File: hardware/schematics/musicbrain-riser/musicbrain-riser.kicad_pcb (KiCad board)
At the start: 2 copper layers, 31 x 80 mm, 2 parts, among them J1 BUS, J2 NAAR FRONT

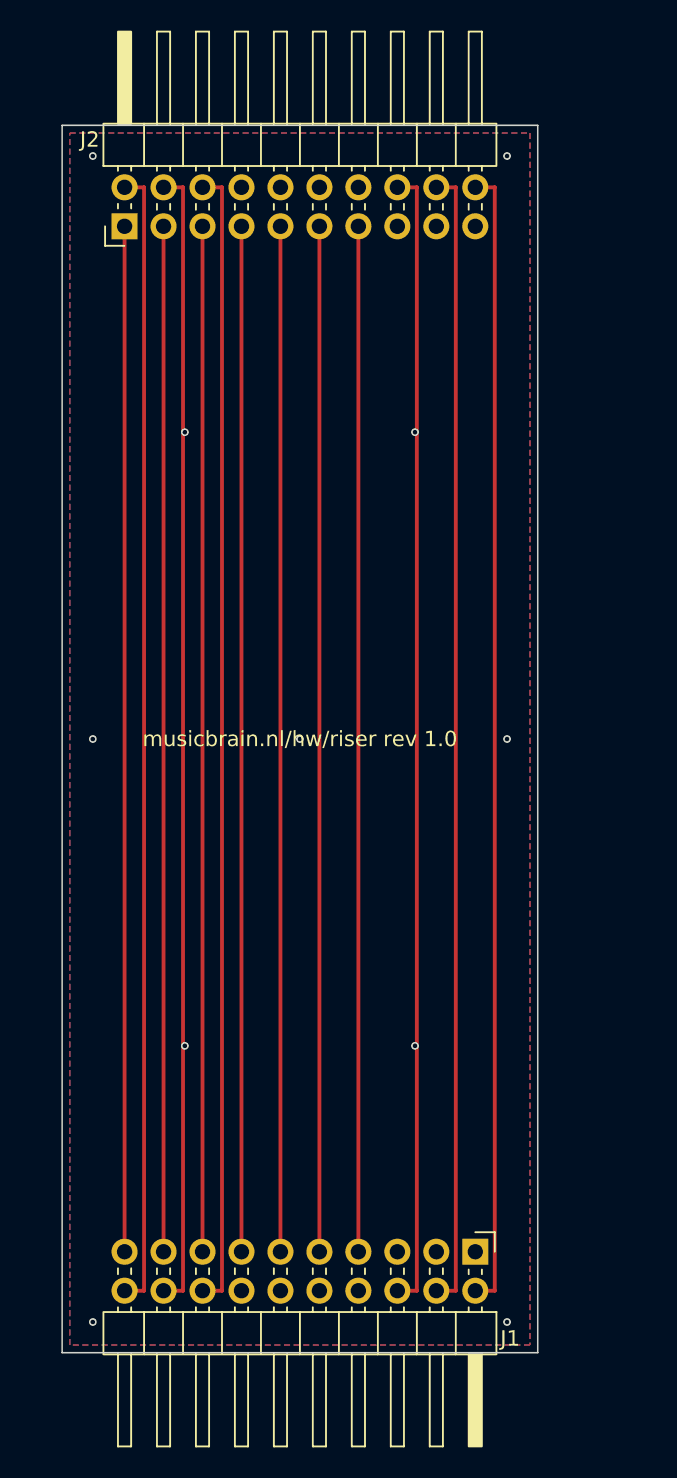
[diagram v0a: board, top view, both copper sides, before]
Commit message: Gen 2 stap 3b/3c: riser + potriser rev 2.0 (2x12, H=50) DRC 0/0
riser: 40x50, hele 2x12-bus 1-op-1 omhoog incl. de audio-lijnen ->
ontwikkelbord voor een gedelegeerde Teensy/FPGA. x-matching schaalt mee:
J2-pin q draagt slotfunctie (24-q) oneven / (26-q) even.

potriser: 28x80 -> 80x50, J1 2x12; koper via freerouting i.p.v. handlanen
(1 unrouted -> snap_stubs dichtte 'm). Front-contract 1x10 ongewijzigd.

Meetvondst: de connector-bodies hangen bewust OVER de bordrand (zo mateert
de kaart met de socket eronder) -- dus de vrije kernband bij H=50 is 33,3 mm,
niet 18,8 zoals ik eerst schatte. Daarmee komt elke kaart op 80x50 uit op
5-16% dichtheid (adc8, de drukste: 15,6%) -- lager dan de huidige ~17% op
80 mm hoog. H=50 is dus ruim haalbaar voor alle kaarten.

Alle drie de risers: ERC 0 / netcheck OK / DRC 0/0.

Co-Authored-By: Claude Fable 5 <noreply@anthropic.com>
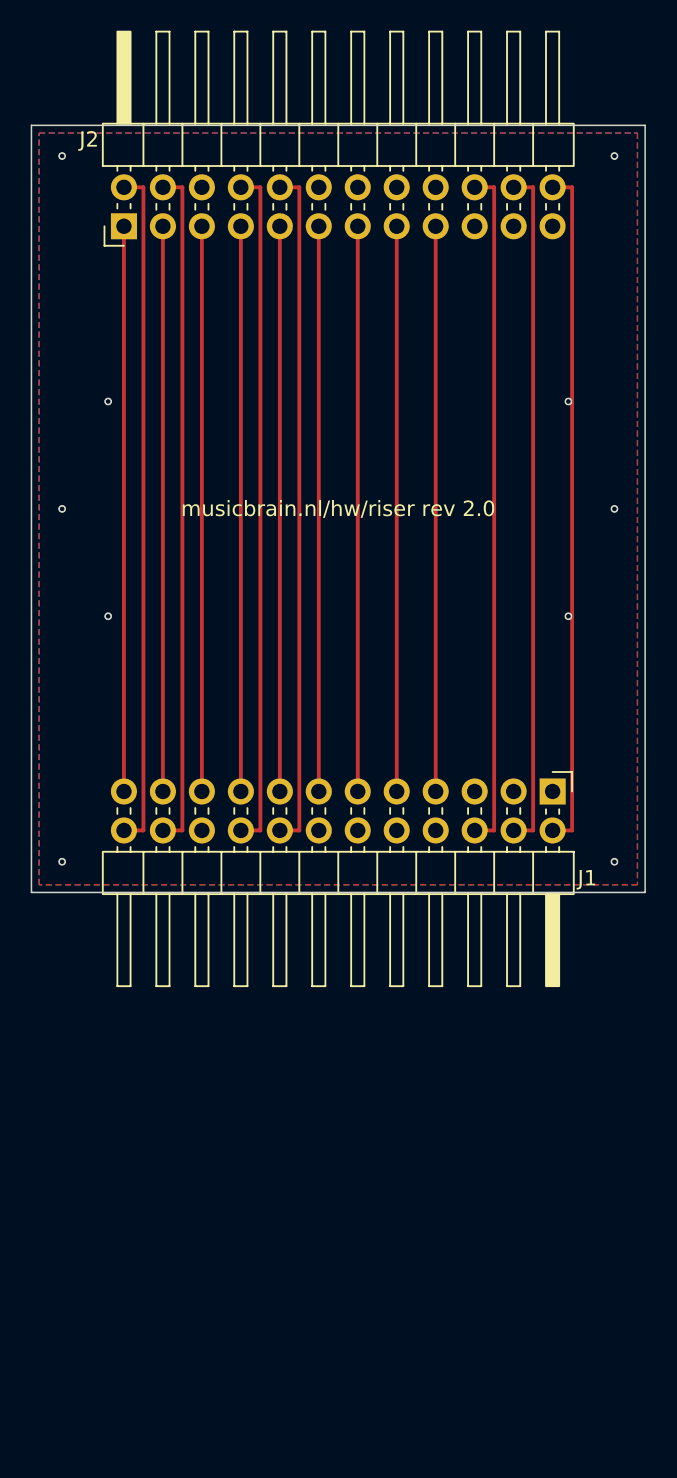
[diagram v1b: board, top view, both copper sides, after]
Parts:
- J1, J2: footprint Connector_PinHeader_2.54mm:PinHeader_2x10_P2.54mm_Horizontal -> Connector_PinHeader_2.54mm:PinHeader_2x12_P2.54mm_Horizontal
- moved J1 30.4 mm to (134.0, 143.4)
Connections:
- J1 pad 20: /SPARE2 -> GND
- J2 pad 1: /SPARE1 -> /LRCLK
- J2 pad 10: GND -> /IRQ
- J2 pad 11: /MOSI -> /CS
- J2 pad 13: /SCLK -> /MISO
- J2 pad 15: GND -> /MOSI
- J2 pad 16: +3V3 -> GND
- J2 pad 17: GND -> /SCLK
- J2 pad 18: -12V -> GND
- J2 pad 2: /SPARE2 -> /I2S_DATA
- J2 pad 20: +12V -> +3V3
- J2 pad 3: /SDA -> /MCLK
- J2 pad 4: /SCL -> /BCLK
- J2 pad 5: /LDAC -> /SPARE1
- J2 pad 6: /IRQ -> GND
- J2 pad 7: /CS -> /SDA
- J2 pad 8: GND -> /SCL
- J2 pad 9: /MISO -> /LDAC
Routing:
- net /SPARE2: track 74.5 -> 0.00 mm
- net /BCLK: track 0.00 -> 44.5 mm
- net /I2S_DATA: track 0.00 -> 44.5 mm
- net /MCLK: track 0.00 -> 36.8 mm
- net /LRCLK: track 0.00 -> 36.8 mm
- net -12V: track 74.5 -> 44.5 mm
- net /SPARE1: track 66.8 -> 36.8 mm
- net /SDA: track 66.8 -> 36.8 mm
- net /SCLK: track 66.8 -> 36.8 mm
- net /SCL: track 74.5 -> 44.5 mm
- net /MOSI: track 66.8 -> 36.8 mm
- net /MISO: track 66.8 -> 36.8 mm
- net /LDAC: track 66.8 -> 36.8 mm
- net /IRQ: track 74.5 -> 44.5 mm
- net /CS: track 66.8 -> 36.8 mm
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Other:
- board size 31 x 80 mm -> 40 x 50 mm
- board text added: "musicbrain.nl/hw/riser rev 2.0"
- board text removed: "musicbrain.nl/hw/riser rev 1.0"

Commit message: gen 2: kaarthoogte 50 -> 45 mm; potriser-herroute (U1 rot 270)
- bus.py: H=45 (band 30,84 mm = bewezen gen-1-dichtheid)
- gen_riser/gen_i2criser/gen_potriser: y-literals geparametriseerd op
  bus.BY0/BY1; potriser leest nu ook gnd_stitch.json in
- potriser: U1 rot 90 -> 270 (kanalen noord, SPI+GND zuid) - bij rot 90
  wikkelden de wiper-banen zich om pad 14 (AGND) en raakte die los van
  het vlak; nieuwe freerouting (0 unrouted) + 1 hechtvia
- alle drie risers: ERC 0, netcheck OK, DRC 0/0 op 40x45 (potriser 80x45)
- docs: spi-bus-spec + systeem-v3-plan H=50 -> H=45, jack4-kabelnotitie

Co-Authored-By: Claude Fable 5 <noreply@anthropic.com>
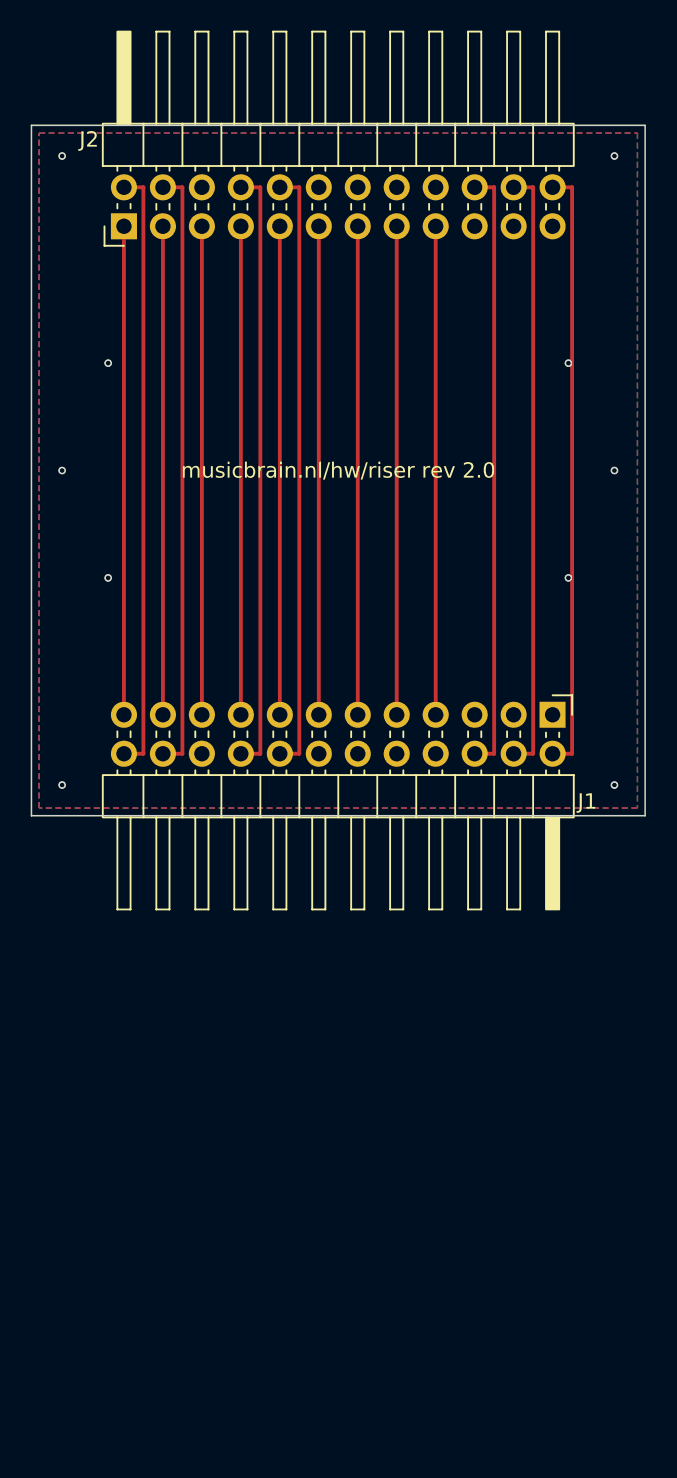
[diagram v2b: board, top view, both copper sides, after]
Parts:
- moved J1 5.00 mm to (134.0, 138.4)
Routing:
- net /SPARE1: track 36.8 -> 31.8 mm
- net /SDA: track 36.8 -> 31.8 mm
- net /SCLK: track 36.8 -> 31.8 mm
- net /SCL: track 44.5 -> 39.5 mm
- net /MOSI: track 36.8 -> 31.8 mm
- net /MISO: track 36.8 -> 31.8 mm
- net /MCLK: track 36.8 -> 31.8 mm
- net /LRCLK: track 36.8 -> 31.8 mm
- net /LDAC: track 36.8 -> 31.8 mm
- net /IRQ: track 44.5 -> 39.5 mm
- net /I2S_DATA: track 44.5 -> 39.5 mm
- net /CS: track 36.8 -> 31.8 mm
- net /BCLK: track 44.5 -> 39.5 mm
- net -12V: track 44.5 -> 39.5 mm
- net +3V3: track 44.5 -> 39.5 mm
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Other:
- board size 40 x 50 mm -> 40 x 45 mm
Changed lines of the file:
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@@
   (net 17 "GND")
   (footprint "Connector_PinHeader_2.54mm:PinHeader_2x12_P2.54mm_Horizontal"
-    (at 133.97 143.42 270)
+    (at 133.97 138.42 270)
     (layer "F.Cu")
     (descr "Through hole angled pin header, 2x12, 2.54mm pitch, 6mm pin length, double rows")
@@
     )
   )
-  (segment (start 133.97 145.96) (end 135.24 145.96) (width 0.25) (layer "F.Cu") (net 1))
-  (segment (start 135.24 145.96) (end 135.24 104.04) (width 0.25) (layer "F.Cu") (net 1))
+  (segment (start 133.97 140.96) (end 135.24 140.96) (width 0.25) (layer "F.Cu") (net 1))
+  (segment (start 135.24 140.96) (end 135.24 104.04) (width 0.25) (layer "F.Cu") (net 1))
   (segment (start 135.24 104.04) (end 133.97 104.04) (width 0.25) (layer "F.Cu") (net 1))
-  (segment (start 131.43 145.96) (end 132.7 145.96) (width 0.25) (layer "F.Cu") (net 3))
-  (segment (start 132.7 145.96) (end 132.7 104.04) (width 0.25) (layer "F.Cu") (net 3))
+  (segment (start 131.43 140.96) (end 132.7 140.96) (width 0.25) (layer "F.Cu") (net 3))
+  (segment (start 132.7 140.96) (end 132.7 104.04) (width 0.25) (layer "F.Cu") (net 3))
   (segment (start 132.7 104.04) (end 131.43 104.04) (width 0.25) (layer "F.Cu") (net 3))
-  (segment (start 128.89 145.96) (end 130.16 145.96) (width 0.25) (layer "F.Cu") (net 2))
-  (segment (start 130.16 145.96) (end 130.16 104.04) (width 0.25) (layer "F.Cu") (net 2))
+  (segment (start 128.89 140.96) (end 130.16 140.96) (width 0.25) (layer "F.Cu") (net 2))
+  (segment (start 130.16 140.96) (end 130.16 104.04) (width 0.25) (layer "F.Cu") (net 2))
   (segment (start 130.16 104.04) (end 128.89 104.04) (width 0.25) (layer "F.Cu") (net 2))
-  (segment (start 126.35 143.42) (end 126.35 106.58) (width 0.25) (layer "F.Cu") (net 14))
-  (segment (start 123.81 143.42) (end 123.81 106.58) (width 0.25) (layer "F.Cu") (net 12))
-  (segment (start 121.27 143.42) (end 121.27 106.58) (width 0.25) (layer "F.Cu") (net 11))
-  (segment (start 118.73 143.42) (end 118.73 106.58) (width 0.25) (layer "F.Cu") (net 5))
-  (segment (start 116.19 143.42) (end 116.19 106.58) (width 0.25) (layer "F.Cu") (net 8))
-  (segment (start 116.19 145.96) (end 117.46 145.96) (width 0.25) (layer "F.Cu") (net 7))
-  (segment (start 117.46 145.96) (end 117.46 104.04) (width 0.25) (layer "F.Cu") (net 7))
+  (segment (start 126.35 138.42) (end 126.35 106.58) (width 0.25) (layer "F.Cu") (net 14))
+  (segment (start 123.81 138.42) (end 123.81 106.58) (width 0.25) (layer "F.Cu") (net 12))
+  (segment (start 121.27 138.42) (end 121.27 106.58) (width 0.25) (layer "F.Cu") (net 11))
+  (segment (start 118.73 138.42) (end 118.73 106.58) (width 0.25) (layer "F.Cu") (net 5))
+  (segment (start 116.19 138.42) (end 116.19 106.58) (width 0.25) (layer "F.Cu") (net 8))
+  (segment (start 116.19 140.96) (end 117.46 140.96) (width 0.25) (layer "F.Cu") (net 7))
+  (segment (start 117.46 140.96) (end 117.46 104.04) (width 0.25) (layer "F.Cu") (net 7))
   (segment (start 117.46 104.04) (end 116.19 104.04) (width 0.25) (layer "F.Cu") (net 7))
-  (segment (start 113.65 143.42) (end 113.65 106.58) (width 0.25) (layer "F.Cu") (net 15))
-  (segment (start 113.65 145.96) (end 114.92 145.96) (width 0.25) (layer "F.Cu") (net 13))
-  (segment (start 114.92 145.96) (end 114.92 104.04) (width 0.25) (layer "F.Cu") (net 13))
+  (segment (start 113.65 138.42) (end 113.65 106.58) (width 0.25) (layer "F.Cu") (net 15))
+  (segment (start 113.65 140.96) (end 114.92 140.96) (width 0.25) (layer "F.Cu") (net 13))
+  (segment (start 114.92 140.96) (end 114.92 104.04) (width 0.25) (layer "F.Cu") (net 13))
   (segment (start 114.92 104.04) (end 113.65 104.04) (width 0.25) (layer "F.Cu") (net 13))
-  (segment (start 111.11 143.42) (end 111.11 106.58) (width 0.25) (layer "F.Cu") (net 16))
-  (segment (start 108.57 143.42) (end 108.57 106.58) (width 0.25) (layer "F.Cu") (net 10))
-  (segment (start 108.57 145.96) (end 109.84 145.96) (width 0.25) (layer "F.Cu") (net 4))
-  (segment (start 109.84 145.96) (end 109.84 104.04) (width 0.25) (layer "F.Cu") (net 4))
+  (segment (start 111.11 138.42) (end 111.11 106.58) (width 0.25) (layer "F.Cu") (net 16))
+  (segment (start 108.57 138.42) (end 108.57 106.58) (width 0.25) (layer "F.Cu") (net 10))
+  (segment (start 108.57 140.96) (end 109.84 140.96) (width 0.25) (layer "F.Cu") (net 4))
+  (segment (start 109.84 140.96) (end 109.84 104.04) (width 0.25) (layer "F.Cu") (net 4))
   (segment (start 109.84 104.04) (end 108.57 104.04) (width 0.25) (layer "F.Cu") (net 4))
-  (segment (start 106.03 143.42) (end 106.03 106.58) (width 0.25) (layer "F.Cu") (net 9))
-  (segment (start 106.03 145.96) (end 107.3 145.96) (width 0.25) (layer "F.Cu") (net 6))
-  (segment (start 107.3 145.96) (end 107.3 104.04) (width 0.25) (layer "F.Cu") (net 6))
+  (segment (start 106.03 138.42) (end 106.03 106.58) (width 0.25) (layer "F.Cu") (net 9))
+  (segment (start 106.03 140.96) (end 107.3 140.96) (width 0.25) (layer "F.Cu") (net 6))
+  (segment (start 107.3 140.96) (end 107.3 104.04) (width 0.25) (layer "F.Cu") (net 6))
   (segment (start 107.3 104.04) (end 106.03 104.04) (width 0.25) (layer "F.Cu") (net 6))
   (via (at 102 102) (size 0.5) (drill 0.3) (layers "F.Cu" "B.Cu") (net 17))
   (via (at 138 102) (size 0.5) (drill 0.3) (layers "F.Cu" "B.Cu") (net 17))
-  (via (at 102 148) (size 0.5) (drill 0.3) (layers "F.Cu" "B.Cu") (net 17))
-  (via (at 138 148) (size 0.5) (drill 0.3) (layers "F.Cu" "B.Cu") (net 17))
-  (via (at 102 125) (size 0.5) (drill 0.3) (layers "F.Cu" "B.Cu") (net 17))
-  (via (at 138 125) (size 0.5) (drill 0.3) (layers "F.Cu" "B.Cu") (net 17))
-  (via (at 105 118) (size 0.5) (drill 0.3) (layers "F.Cu" "B.Cu") (net 17))
-  (via (at 135 118) (size 0.5) (drill 0.3) (layers "F.Cu" "B.Cu") (net 17))
-  (via (at 105 132) (size 0.5) (drill 0.3) (layers "F.Cu" "B.Cu") (net 17))
-  (via (at 135 132) (size 0.5) (drill 0.3) (layers "F.Cu" "B.Cu") (net 17))
-  (gr_rect (start 100.0 100.0) (end 140.0 150.0)
+  (via (at 102 143) (size 0.5) (drill 0.3) (layers "F.Cu" "B.Cu") (net 17))
+  (via (at 138 143) (size 0.5) (drill 0.3) (layers "F.Cu" "B.Cu") (net 17))
+  (via (at 102 122.5) (size 0.5) (drill 0.3) (layers "F.Cu" "B.Cu") (net 17))
+  (via (at 138 122.5) (size 0.5) (drill 0.3) (layers "F.Cu" "B.Cu") (net 17))
+  (via (at 105 115.5) (size 0.5) (drill 0.3) (layers "F.Cu" "B.Cu") (net 17))
+  (via (at 135 115.5) (size 0.5) (drill 0.3) (layers "F.Cu" "B.Cu") (net 17))
+  (via (at 105 129.5) (size 0.5) (drill 0.3) (layers "F.Cu" "B.Cu") (net 17))
+  (via (at 135 129.5) (size 0.5) (drill 0.3) (layers "F.Cu" "B.Cu") (net 17))
+  (gr_rect (start 100.0 100.0) (end 140.0 145.0)
     (stroke (width 0.1) (type default)) (fill none)
     (layer "Edge.Cuts"))
-  (gr_text "musicbrain.nl/hw/riser rev 2.0" (at 120 125 0) (layer "F.SilkS")
+  (gr_text "musicbrain.nl/hw/riser rev 2.0" (at 120 122.5 0) (layer "F.SilkS")
     (effects (font (size 1 1) (thickness 0.15))))
   (zone (net 17) (net_name "GND") (layer "F.Cu")
@@
     (polygon (pts
       (xy 100.5 100.5) (xy 139.5 100.5)
-      (xy 139.5 149.5) (xy 100.5 149.5)
+      (xy 139.5 144.5) (xy 100.5 144.5)
     ))
   )
@@
     (polygon (pts
       (xy 100.5 100.5) (xy 139.5 100.5)
-      (xy 139.5 149.5) (xy 100.5 149.5)
+      (xy 139.5 144.5) (xy 100.5 144.5)
     ))
   )
